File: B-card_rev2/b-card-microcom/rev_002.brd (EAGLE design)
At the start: 88.9 x 50.8 mm, 47 parts, among them IC1 DMN2041L-7, IC2 DMN2041L-7, IC3 DMN2041L-7, IC4 AZ1117I, IC5 AZ1117I, IC6 AZ1117I, IC7 TLV74033, J1 10118192-0002LF, SW1 B3AL-1000P, U1 ATMEGA32U4-MU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

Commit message: update
this should work, Kinda feel like i should be pushing more current though the elements, but its rev 2, we will see.

Vreg & resistors should stay below the thermal limit. The only thing that should get hot is the activation wire..... mfets should stay cool too i hope.
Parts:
- added C9: 1uF, rcl:C0603
- D1, D2: value (none) -> LSM115JE3; device diode:MINIMELF -> diode:DO214BA
- IC4, IC5, IC6: value AZ1117I -> AZ1117IH-5.0
- IC7: value TLV74033 -> AZ1117IH-3.3; device v-reg-micrel:SOT23-5 -> v-reg:SOT223
- moved IC7 46.8 mm to (34.3, 44.5)
- moved D1 9.67 mm to (59.7, 6.35)
- moved D2 7.73 mm to (48.3, 3.81)
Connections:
- net +3V3: now also IC7.4; no longer IC7.5
- net +4.1V: now also C9.1; no longer IC7.1
- net GND: now also C9.2, IC7.1; no longer IC7.2

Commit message: renum
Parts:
- C1: value 10uF -> 1uF
- C11: value 1uF -> 10uF
- C2, C9: value 1uF -> 0.1uF
- C3, C8: value 0.1uF -> 1uF
- IC1, IC2, IC3: value DMN2041L-7 -> AZ1117IH-5.0; device ds31126:SOT23 -> v-reg:SOT223
- IC4, IC5, IC6: value AZ1117IH-5.0 -> DMN2041L-7; device v-reg:SOT223 -> ds31126:SOT23
- PAD1, PAD4: value WIREPADSMD1,27-254 -> WIREPADSMD5-2,5; device wirepad:SMD1,27-2,54 -> wirepad:5-2,5
- PAD10, PAD9: value WIREPADSMD5-2,5 -> WIREPADSMD1,27-254; device wirepad:5-2,5 -> wirepad:SMD1,27-2,54
- PAD2, PAD3: value WIREPADSMD1,27-254 -> WIREPAD2,54/0,9; device wirepad:SMD1,27-2,54 -> wirepad:2,54/0,9
- PAD7, PAD8: value WIREPAD2,54/0,9 -> WIREPADSMD1,27-254; device wirepad:2,54/0,9 -> wirepad:SMD1,27-2,54
- R1, R2: value 22 -> 11; device rcl:R0603 -> rcl:R2512
- R11: value 100k -> 600
- R12, R7: value 11 -> 100k; device rcl:R2512 -> rcl:R0603
- R3: value 100k -> 11; device rcl:R0603 -> rcl:R2512
- R5: value 11 -> 22; device rcl:R2512 -> rcl:R0603
- R6: value 600 -> 22
- moved IC1 61.0 mm to (11.4, 17.8)
- moved IC6 61.0 mm to (71.1, 30.5)
- moved IC3 58.4 mm to (15.2, 44.5)
- moved IC4 58.4 mm to (73.7, 45.7)
- moved PAD10 51.1 mm to (35.6, 10.2)
- moved PAD4 47.5 mm to (85.1, 22.9)
- moved PAD3 45.4 mm to (83.8, 30.5)
- moved PAD8 45.4 mm to (43.2, 10.2)
- moved PAD2 44.4 mm to (82.5, 36.8)
- moved PAD7 44.4 mm to (47.0, 10.2)
- moved C11 44.4 mm to (17.8, 8.89)
- moved PAD9 43.4 mm to (39.4, 10.2)
- moved R12 37.6 mm to (61.0, 29.2)
- moved C4 37.2 mm to (61.0, 24.1)
- moved C6 33.3 mm to (61.0, 19.1)
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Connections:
- net !RST: now also PAD6.1, R10.1; no longer PAD1.1, R4.1
- net +3V3: now also C4.1, C6.1, PAD5.1, R10.2, R12.2; no longer C1.1, C10.1, PAD6.1, R11.2, R4.2
- net +4.1V: now also C3.1; no longer C9.1
- net +5V: now also C1.1, IC4.D, IC5.D, IC6.D, R1.2, R2.2, R3.2; no longer C4.1, IC1.D, IC2.D, IC3.D, R12.2, R5.2, R7.2
- net +8V: now also C8.1, IC1.3, IC2.3, IC3.3, PAD1.1, PAD2.1; no longer C6.1, IC4.3, IC5.3, IC6.3, PAD7.1, PAD9.1
- net D+: now also R5.1; no longer R2.1
- net D-: now also R6.1; no longer R1.1
- net D10: now also IC5.G, R8.2; no longer IC2.G, R9.2
- net D11: now also C9.1, R12.1; no longer C8.1, R11.1
- net D8: now also IC4.G, R4.2; no longer IC3.G, R10.2
- net D9: now also IC6.G, R9.2; no longer IC1.G, R8.2
- net E1: now also IC4.S; no longer IC3.S
- net E2: now also IC5.S; no longer IC2.S
- net E3: now also IC6.S; no longer IC1.S
- net GND: now also IC1.1, IC2.1, IC3.1, PAD3.1, PAD4.1, R11.1, R4.1, R7.1; no longer IC4.1, IC5.1, IC6.1, PAD5.1, PAD8.1, R10.1, R3.1, R6.1
- net MISO: now also PAD9.1; no longer PAD4.1
- net MOSI: now also PAD8.1; no longer PAD3.1
- net N$1: now also R6.2; no longer R1.2
- net N$11: now also IC1.4, R1.1; no longer IC6.4, R12.1
- net N$2: now also C10.1; no longer C2.1
- net N$3: now also R5.2; no longer R2.2
- net N$4: now also C2.1, R7.2; no longer C3.1, R3.2
- net N$6: now also R11.2; no longer R6.2
- net N$7: now also IC3.4, R3.1; no longer IC4.4, R7.1
- net N$9: now also IC2.4, R2.1; no longer IC5.4, R5.1
- net SCK: now also PAD7.1; no longer PAD2.1

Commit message: layout kinda done
I'm not 100% happy with everything yet, but it looks like it could work.
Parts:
- added C12, C13, C14, C15, C16: 1uF, rcl:C0603
- moved LED1 66.7 mm to (81.9, 25.4), turned to 180 degrees
- moved IC6 66.3 mm to (7.62, 11.4), turned to 270 degrees
- moved IC4 66.1 mm to (7.62, 42.9), turned to 270 degrees
- moved R4 65.4 mm to (7.30, 45.7), turned to 180 degrees
- moved C11 61.8 mm to (73.7, 35.2)
- moved IC7 56.0 mm to (83.8, 18.4), turned to 90 degrees
- moved SW1 52.1 mm to (27.3, 6.99)
- moved C8 52.0 mm to (74.9, 4.45), turned to 270 degrees
- moved PAD5 50.1 mm to (63.2, 49.2), turned to 180 degrees
- moved PAD9 49.5 mm to (69.8, 49.2)
- moved PAD10 49.2 mm to (65.4, 49.2), turned to 180 degrees
- moved R11 48.7 mm to (85.4, 25.4), turned to 180 degrees
- moved PAD8 48.6 mm to (72.1, 49.2)
- moved C7 48.5 mm to (77.2, 4.45), turned to 270 degrees
- moved C3 48.0 mm to (85.4, 23.2), turned to 180 degrees
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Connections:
- net D+ renamed USBA_P
- net D- renamed USBA_N
- net N$1 renamed USBB_N
- net N$3 renamed USBB_P
- removed net D11: C9.1, R12.1, SW1.2, U1.12
- new net D6: IC4.G, R4.2, U1.27
- new net VBUS: D1.A, J1.1, U1.7
- net +3V3: now also C14.1, C15.1, C16.1
- net +5V: now also C12.1, C13.1; no longer D1.A, J1.1, U1.7
- net D10: now also C9.1, R12.1, SW1.2; no longer IC5.G, R8.2
- net D8: now also IC5.G, R8.2; no longer IC4.G, R4.2
- net GND: now also C12.2, C13.2, C14.2, C15.2, C16.2
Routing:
- net +3V3: track 0.00 -> 132.1 mm, vias 0 -> 7
- net D9: track 0.00 -> 68.8 mm, vias 0 -> 2
- net D6: track 0.00 -> 65.5 mm, vias 0 -> 2
- net D8: track 0.00 -> 65.3 mm, vias 0 -> 2
- net D10: track 0.00 -> 47.1 mm, vias 0 -> 2
- net GND: track 0.00 -> 40.4 mm, vias 0 -> 7
- net VBUS: track 0.00 -> 39.8 mm, vias 0 -> 3
- net N$4: track 0.00 -> 18.2 mm
- net +4.1V: track 0.00 -> 17.1 mm
- net SCK: track 0.00 -> 14.7 mm
- net MOSI: track 0.00 -> 14.1 mm
- net MISO: track 0.00 -> 13.9 mm
- net !RST: track 0.00 -> 12.6 mm, vias 0 -> 2
- net USBA_N: track 0.00 -> 12.4 mm
- net +8V: track 0.00 -> 10.6 mm
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- added copper zone on layer 1, net +5V
- added copper zone on layer 1, net +8V
- added copper zone on layer 1, net D10
- added copper zone on layer 1, net E1
- added copper zone on layer 1, net E2
- added copper zone on layer 1, net E3
- added copper zone on layer 1, net GND
- added copper zone on layer 16, net GND

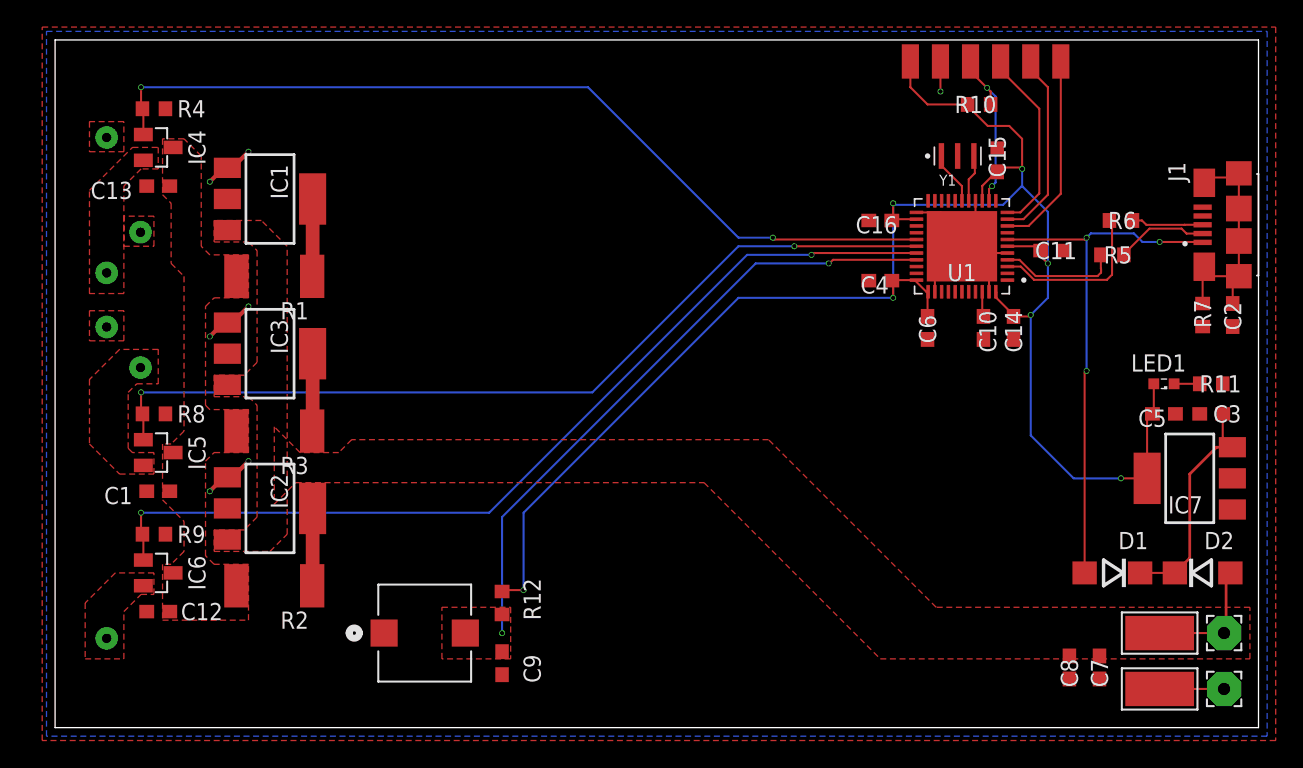
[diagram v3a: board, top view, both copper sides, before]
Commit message: rev 2 90% done
I need to give everything a once over before fab, and throw together a parts list.
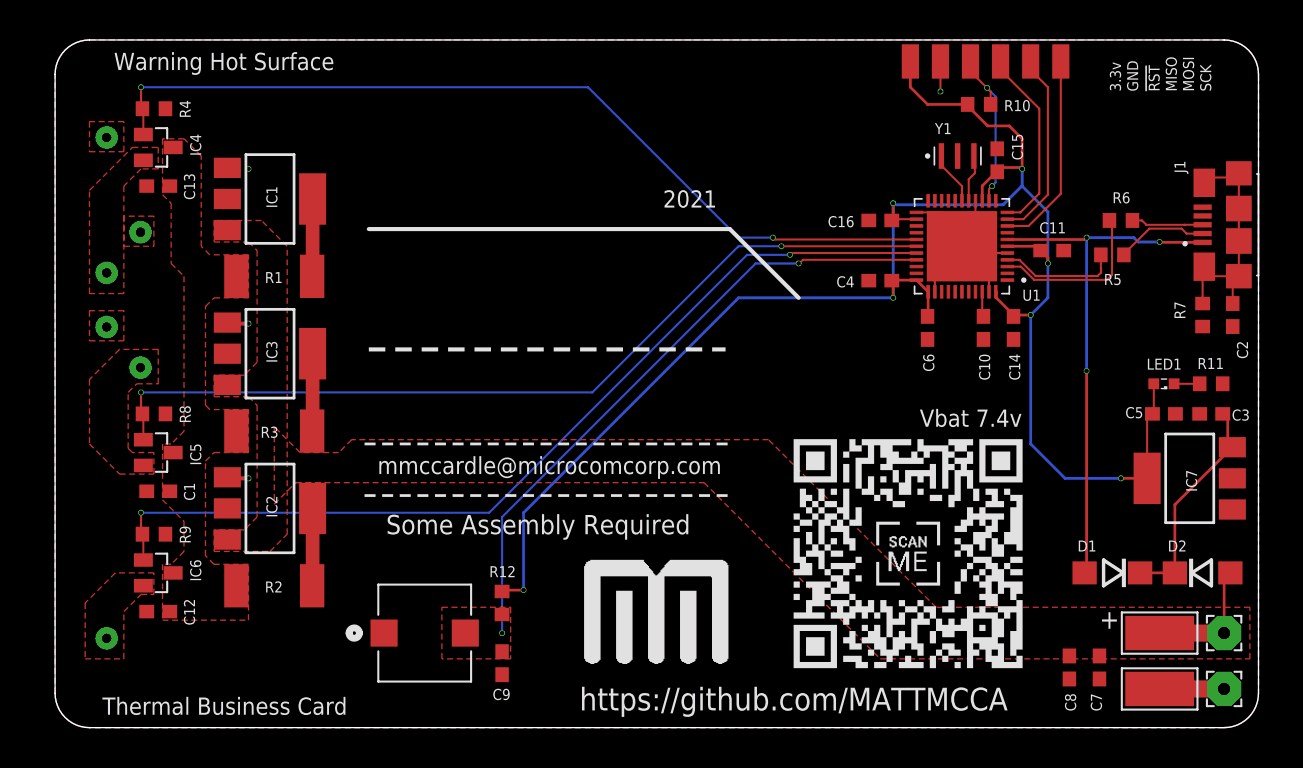
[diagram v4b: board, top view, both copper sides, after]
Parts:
- added U$1: (no value), b-card-link:LINK
- added U$2: (no value), b-card-link:MCOM
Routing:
- net GND: track 40.4 -> 30.5 mm, vias 7 -> 4
- net +8V: track 10.6 -> 9.40 mm
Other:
- outline, holes or cut-outs redrawn
- board text added: "!RST"
- board text added: "+"
- board text added: "2021"
- board text added: "3.3v"
- board text added: "Cell: 740-975-3595"
- board text added: "GND"
- board text added: "MISO"
- board text added: "MOSI"
- board text added: "Matthew McCardle"
- board text added: "Microcom Corporation"
- board text added: "SCK"
- board text added: "Some Assembly Required"
- board text added: "Support Engineer"
- board text added: "Thermal Business Card"
- board text added: "Vbat 7.4v"
- board text added: "Warning Hot Surface"
- board text added: "Work: 740-548-6262"
- board text added: "https://github.com/MATTMCCA"
- board text added: "mmccardle@microcomcorp.com"

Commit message: update
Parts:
- C14, C15, C16, C4, C6: value 1uF -> 0.1uF
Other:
- board text added: "https://www.microcomcorp.com"
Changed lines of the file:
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@@
 </layers>
 <board>
-<fusionsync huburn="a.YnVzaW5lc3M6bWljcm9jb21jb3Jw" projecturn="a.YnVzaW5lc3M6bWljcm9jb21jb3JwI0QyMDIxMDYxMDQxOTQ4MzU4MQ" f3durn="urn:adsk.wipprod:dm.lineage:hVZSTlcWSTCayl2Rg-kBcg" pcbguid="38324b95-f16b-4be6-b83f-e768f8fb8096" lastpulledtime="" lastsyncedchangeguid="" latestrevisionid="6cf69bb5-ddfe-4a12-9340-ddf4eb80fb93" lastsyncedrevisionid="6cf69bb5-ddfe-4a12-9340-ddf4eb80fb93" lastboardhashguid="6470bd19-9ceb-2cb8-f10b-da75035a346b" lastpushedtime="2021-12-27T14:39:14Z" linktopcb3d="true"/>
+<fusionsync huburn="a.YnVzaW5lc3M6bWljcm9jb21jb3Jw" projecturn="a.YnVzaW5lc3M6bWljcm9jb21jb3JwI0QyMDIxMDYxMDQxOTQ4MzU4MQ" f3durn="urn:adsk.wipprod:dm.lineage:hVZSTlcWSTCayl2Rg-kBcg" pcbguid="" lastpulledtime="" lastsyncedchangeguid="" latestrevisionid="6cf69bb5-ddfe-4a12-9340-ddf4eb80fb93" lastsyncedrevisionid="6cf69bb5-ddfe-4a12-9340-ddf4eb80fb93" lastboardhashguid="6470bd19-9ceb-2cb8-f10b-da75035a346b" lastpushedtime="2021-12-27T14:39:14Z" linktopcb3d="true"/>
 <plain>
 <wire x1="0" y1="48.26" x2="0" y2="2.54" width="0" layer="20"/>
@@
 <text x="23.1775" y="38.4175" size="3.81" layer="29" font="vector" ratio="10">Matthew
 McCardle</text>
-<text x="22.86" y="29.845" size="2.54" layer="29" font="vector" ratio="10">Support Engineer</text>
+<text x="22.86" y="30.7975" size="2.54" layer="29" font="vector" ratio="10">Support Engineer</text>
 <wire x1="23.1775" y1="36.83" x2="49.8475" y2="36.83" width="0.3048" layer="21"/>
 <wire x1="49.8475" y1="36.83" x2="54.9275" y2="31.75" width="0.3048" layer="21"/>
-<wire x1="23.1775" y1="27.94" x2="49.53" y2="27.94" width="0.3048" layer="21" style="dashdot"/>
-<text x="23.1775" y="24.4475" size="1.778" layer="29" font="vector" ratio="10">Work: 740-548-6262</text>
-<text x="24.765" y="21.9075" size="1.778" layer="29" font="vector" ratio="10">Cell: 740-975-3595</text>
-<text x="23.1775" y="33.655" size="1.6764" layer="41" font="vector" ratio="10">Microcom Corporation</text>
-<text x="23.1775" y="33.655" size="1.6764" layer="29" font="vector" ratio="10">Microcom Corporation</text>
+<wire x1="23.1775" y1="29.21" x2="49.53" y2="29.21" width="0.254" layer="21"/>
+<text x="23.495" y="26.67" size="1.778" layer="29" font="vector" ratio="10">Work: 740-548-6262</text>
+<text x="25.0825" y="24.13" size="1.778" layer="29" font="vector" ratio="10">Cell: 740-975-3595</text>
+<text x="23.1775" y="34.29" size="1.6764" layer="29" font="vector" ratio="10">Microcom Corporation</text>
 <text x="38.735" y="1.27" size="1.6764" layer="21" font="vector" ratio="10">https://github.com/MATTMCCA</text>
 <text x="21.59" y="2.2225" size="1.27" layer="21" font="vector" ratio="15" rot="R180">Thermal Business Card</text>
@@
 <text x="20.6375" y="49.8475" size="1.27" layer="21" font="vector" ratio="15" rot="R180">Warning Hot Surface</text>
 <text x="71.4375" y="23.495" size="1.27" layer="21" font="vector" ratio="15" rot="R180">Vbat 7.4v</text>
-<text x="24.4475" y="14.2875" size="1.4224" layer="21" font="vector" ratio="15">Some Assembly Required</text>
-<wire x1="22.86" y1="17.145" x2="49.8475" y2="17.145" width="0.2032" layer="21" style="shortdash"/>
+<text x="24.4475" y="14.9225" size="1.4224" layer="21" font="vector" ratio="15">Some Assembly Required</text>
+<wire x1="22.86" y1="18.0975" x2="49.8475" y2="18.0975" width="0.254" layer="21"/>
 <text x="77.1525" y="7.3025" size="1.4224" layer="21" font="vector" ratio="15">+</text>
-<wire x1="22.86" y1="20.955" x2="49.8475" y2="20.955" width="0.2032" layer="21" style="shortdash"/>
-<text x="23.8125" y="18.7325" size="1.27" layer="21" font="vector" ratio="15">mmccardle@microcomcorp.com</text>
+<wire x1="22.86" y1="20.955" x2="49.8475" y2="20.955" width="0.254" layer="21"/>
+<text x="23.8125" y="21.9075" size="1.27" layer="21" font="vector" ratio="15">mmccardle@microcomcorp.com</text>
+<text x="25.4" y="19.05" size="1.016" layer="21" font="vector" ratio="16">https://www.microcomcorp.com</text>
+<wire x1="49.8475" y1="35.56" x2="56.1975" y2="29.21" width="0.254" layer="21"/>
 </plain>
 <attributes>
@@
 <attribute name="SPICEPREFIX" value="R" x="33.02" y="9.2075" size="1.778" layer="27" rot="R90" display="off"/>
 </element>
-<element name="C4" library="rcl" library_urn="urn:adsk.eagle:library:334" package="C0603" package3d_urn="urn:adsk.eagle:package:23616/2" value="1uF" x="60.96" y="33.02" smashed="yes" rot="R180">
+<element name="C4" library="rcl" library_urn="urn:adsk.eagle:library:334" package="C0603" package3d_urn="urn:adsk.eagle:package:23616/2" value="0.1uF" x="60.96" y="33.02" smashed="yes" rot="R180">
 <attribute name="NAME" x="59.055" y="33.3375" size="0.8128" layer="25" font="vector" ratio="15" rot="R180"/>
 <attribute name="POPULARITY" value="73" x="60.96" y="33.02" size="1.778" layer="27" rot="R180" display="off"/>
 <attribute name="SPICEPREFIX" value="C" x="60.96" y="33.02" size="1.778" layer="27" rot="R180" display="off"/>
 </element>
-<element name="C6" library="rcl" library_urn="urn:adsk.eagle:library:334" package="C0603" package3d_urn="urn:adsk.eagle:package:23616/2" value="1uF" x="64.4525" y="29.5275" smashed="yes" rot="R270">
+<element name="C6" library="rcl" library_urn="urn:adsk.eagle:library:334" package="C0603" package3d_urn="urn:adsk.eagle:package:23616/2" value="0.1uF" x="64.4525" y="29.5275" smashed="yes" rot="R270">
 <attribute name="NAME" x="64.135" y="27.6225" size="0.8128" layer="25" font="vector" ratio="15" rot="R270"/>
 <attribute name="POPULARITY" value="73" x="64.4525" y="29.5275" size="1.778" layer="27" rot="R270" display="off"/>
@@
 <attribute name="SPICEPREFIX" value="C" x="7.62" y="40.005" size="1.778" layer="27" rot="R180" display="off"/>
 </element>
-<element name="C14" library="rcl" library_urn="urn:adsk.eagle:library:334" package="C0603" package3d_urn="urn:adsk.eagle:package:23616/2" value="1uF" x="70.8025" y="29.5275" smashed="yes" rot="R270">
+<element name="C14" library="rcl" library_urn="urn:adsk.eagle:library:334" package="C0603" package3d_urn="urn:adsk.eagle:package:23616/2" value="0.1uF" x="70.8025" y="29.5275" smashed="yes" rot="R270">
 <attribute name="NAME" x="70.485" y="27.6225" size="0.8128" layer="25" font="vector" ratio="15" rot="R270"/>
 <attribute name="POPULARITY" value="73" x="70.8025" y="29.5275" size="1.778" layer="27" rot="R270" display="off"/>
 <attribute name="SPICEPREFIX" value="C" x="70.8025" y="29.5275" size="1.778" layer="27" rot="R270" display="off"/>
 </element>
-<element name="C15" library="rcl" library_urn="urn:adsk.eagle:library:334" package="C0603" package3d_urn="urn:adsk.eagle:package:23616/2" value="1uF" x="69.596" y="41.91" smashed="yes" rot="R90">
+<element name="C15" library="rcl" library_urn="urn:adsk.eagle:library:334" package="C0603" package3d_urn="urn:adsk.eagle:package:23616/2" value="0.1uF" x="69.596" y="41.91" smashed="yes" rot="R90">
 <attribute name="NAME" x="71.501" y="41.91" size="0.8128" layer="25" font="vector" ratio="15" rot="R90"/>
 <attribute name="POPULARITY" value="73" x="69.596" y="41.91" size="1.778" layer="27" rot="R90" display="off"/>
 <attribute name="SPICEPREFIX" value="C" x="69.596" y="41.91" size="1.778" layer="27" rot="R90" display="off"/>
 </element>
-<element name="C16" library="rcl" library_urn="urn:adsk.eagle:library:334" package="C0603" package3d_urn="urn:adsk.eagle:package:23616/2" value="1uF" x="60.96" y="37.465" smashed="yes" rot="R180">
+<element name="C16" library="rcl" library_urn="urn:adsk.eagle:library:334" package="C0603" package3d_urn="urn:adsk.eagle:package:23616/2" value="0.1uF" x="60.96" y="37.465" smashed="yes" rot="R180">
 <attribute name="NAME" x="59.055" y="37.7825" size="0.8128" layer="25" font="vector" ratio="15" rot="R180"/>
 <attribute name="POPULARITY" value="73" x="60.96" y="37.465" size="1.778" layer="27" rot="R180" display="off"/>

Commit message: updated
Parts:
- IC1, IC2, IC3, IC7: device v-reg:SOT223 -> v-reg-edit:SOT223
- LED1: device led:SML0603 -> led_edit:SML0603
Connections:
- net +3V3: now also IC7.2
- net N$11: now also IC1.2
- net N$7: now also IC3.2
- net N$9: now also IC2.2
